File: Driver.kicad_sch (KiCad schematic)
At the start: 24 parts

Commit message: Тестовая версия
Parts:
- R7, R8: value 1.1k -> 10k
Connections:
- net E1 renamed OUT1
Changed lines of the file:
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@@
     )
   )
-  (global_label "E1" (shape input) (at 119.126 150.876 0) (fields_autoplaced)
-    (effects (font (size 1.27 1.27)) (justify left))
-    (property "Intersheet References" "${INTERSHEET_REFS}" (id 0) (at 123.8977 150.7966 0)
+  (global_label "OUT1" (shape input) (at 119.126 150.876 0) (fields_autoplaced)
+    (effects (font (size 1.27 1.27)) (justify left))
+    (property "Intersheet References" "${INTERSHEET_REFS}" (id 0) (at 126.3772 150.7966 0)
       (effects (font (size 1.27 1.27)) (justify left) hide)
     )
@@
     (in_bom yes) (on_board yes)
     (property "Reference" "R8" (id 0) (at 110.236 72.136 0))
-    (property "Value" "1.1k" (id 1) (at 105.918 72.136 90))
+    (property "Value" "10k" (id 1) (at 105.918 72.136 90))
     (property "Footprint" "Resistor_SMD:R_0805_2012Metric_Pad1.20x1.40mm_HandSolder" (id 2) (at 107.95 72.136 0)
       (effects (font (size 1.27 1.27)) hide)
@@
     (in_bom yes) (on_board yes)
     (property "Reference" "R7" (id 0) (at 105.664 148.59 90))
-    (property "Value" "1.1k" (id 1) (at 105.664 150.876 90))
+    (property "Value" "10k" (id 1) (at 105.664 150.876 90))
     (property "Footprint" "Resistor_SMD:R_0805_2012Metric_Pad1.20x1.40mm_HandSolder" (id 2) (at 105.664 150.876 0)
       (effects (font (size 1.27 1.27)) hide)

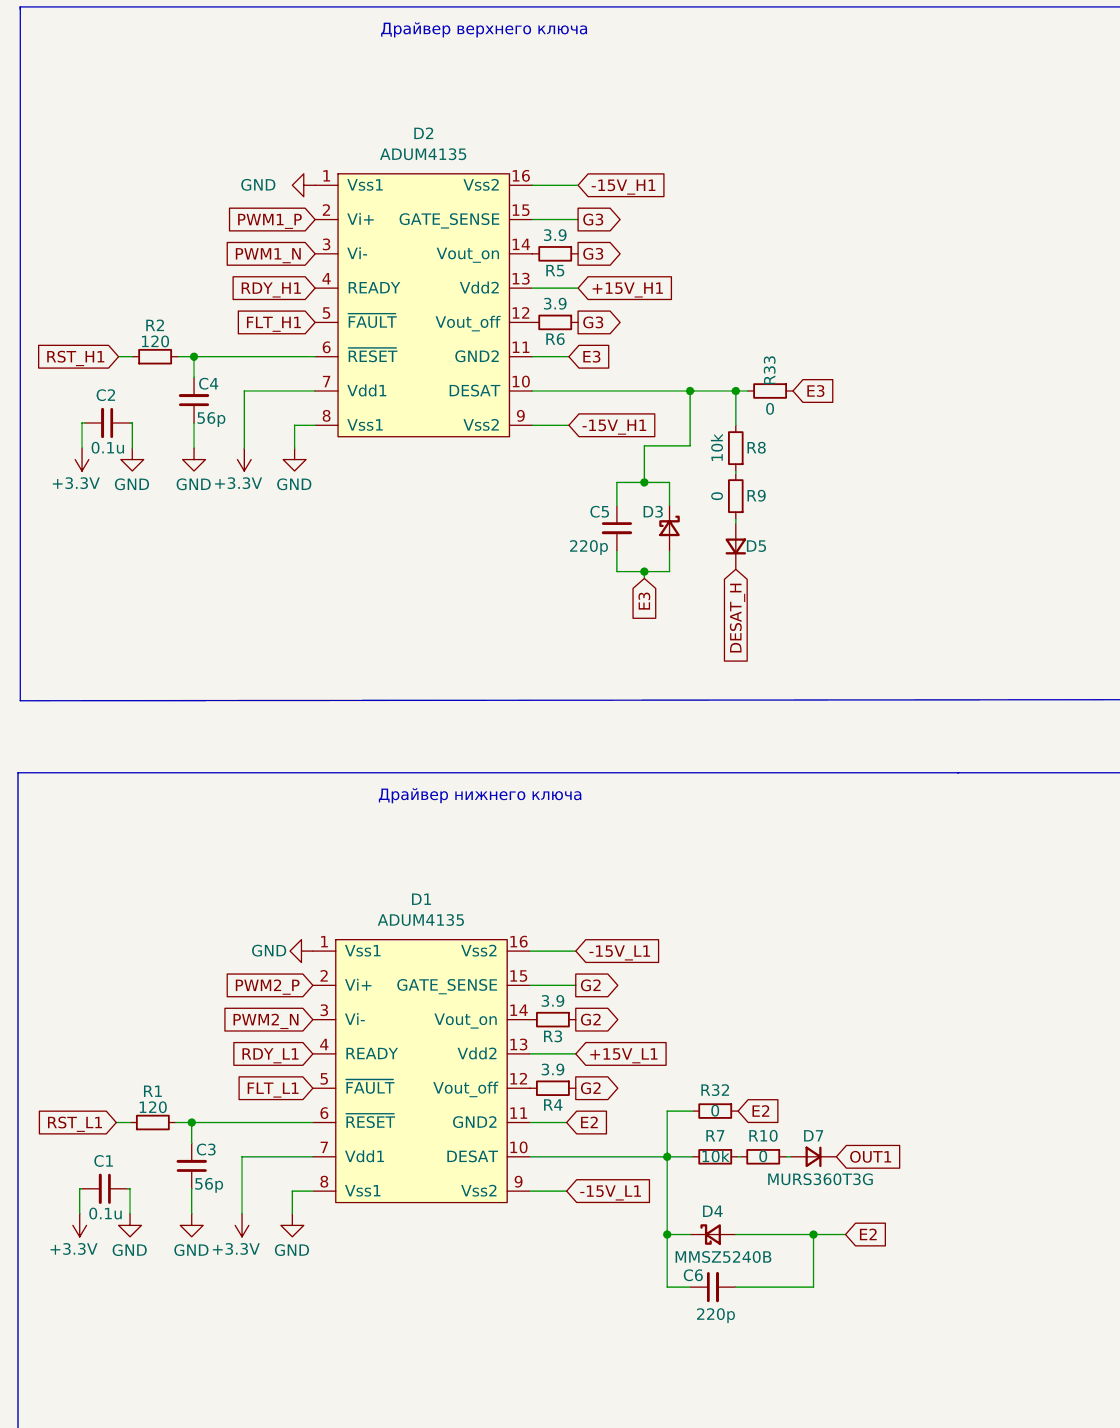
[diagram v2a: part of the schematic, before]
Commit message: Убрал питание 3.3В
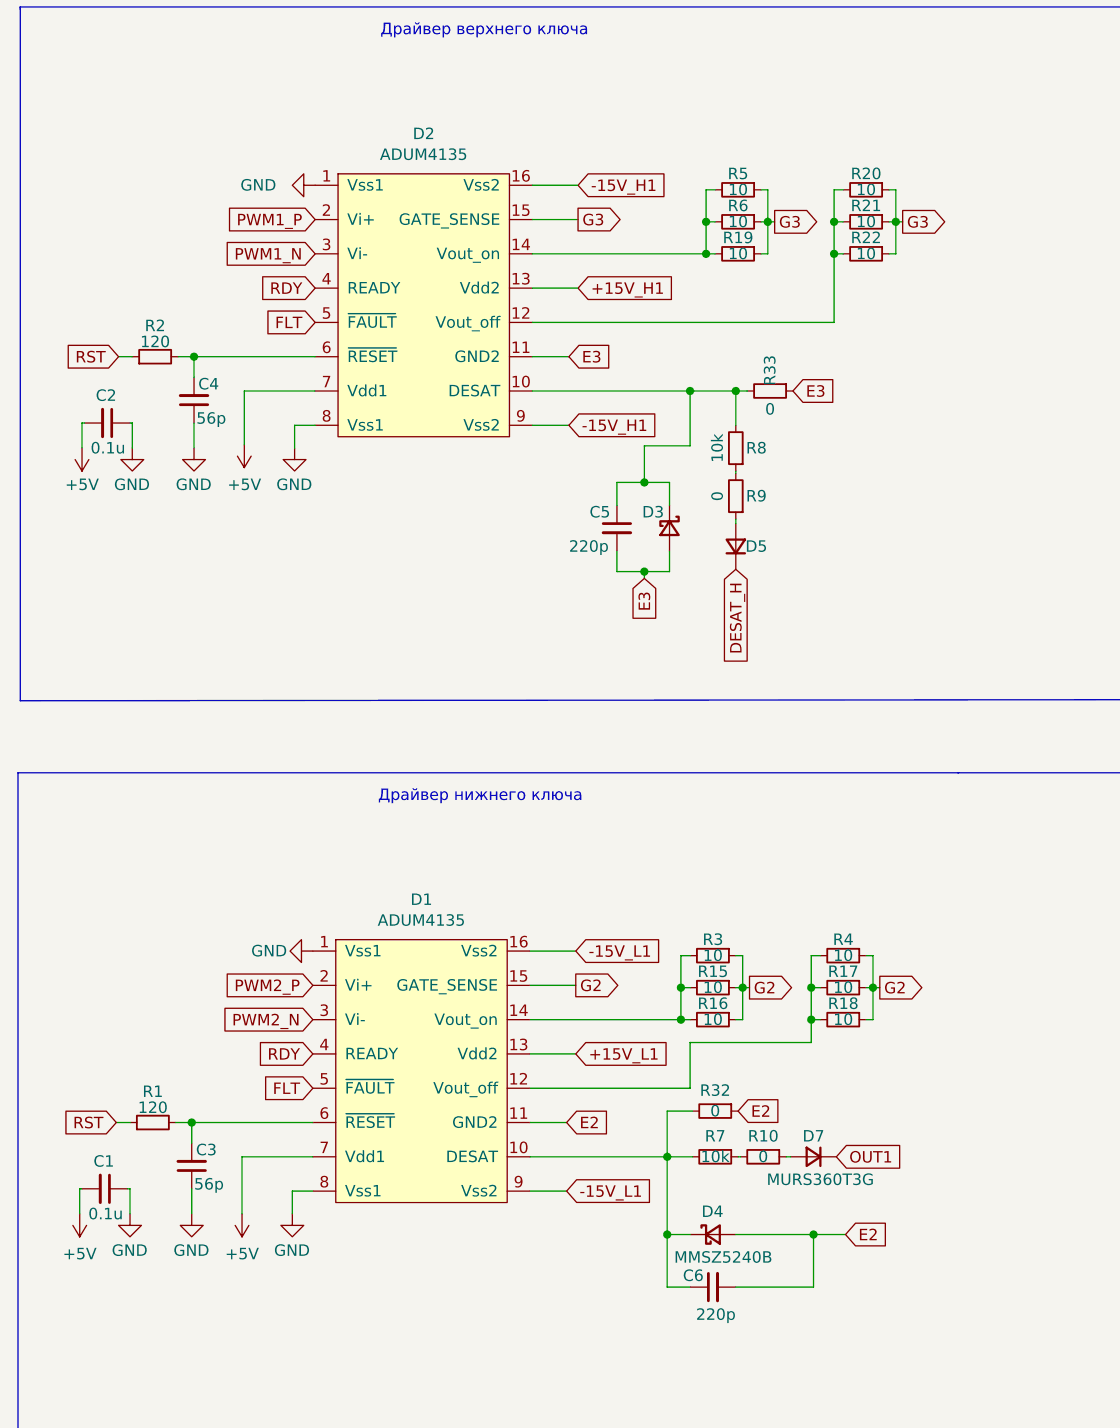
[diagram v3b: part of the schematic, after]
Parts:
- added R15, R16, R17, R18, R19, R20, R21, R22: 10, Resistor_SMD:R_1206_3216Metric_Pad1.30x1.75mm_HandSolder, symbol Device:R_Small
- D5, D7: footprint Diode_SMD:D_SMC -> Diode_SMD:D_SMA
- R3, R4, R5, R6: value 3.9 -> 10; footprint Resistor_SMD:R_2512_6332Metric_Pad1.40x3.35mm_HandSolder -> Resistor_SMD:R_1206_3216Metric_Pad1.30x1.75mm_HandSolder
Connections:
- net FLT_L1 is gone; now on net FLT: D1.5 (~{FAULT})
- net RDY_L1 is gone; now on net RDY: D1.4 (READY)
- net RST_L1 is gone; now on net RST: R1.1
- net G2: now also R15.1, R16.1, R17.1, R18.1
- net G3: now also R19.1, R20.1, R21.1, R22.1
- net at D2.12 (Vout_off): now also R20.2, R21.2, R22.2; no longer R6.2
- net at D1.14 (Vout_on), R3.2: now also R15.2, R16.2
- net at D2.14 (Vout_on), R5.2: now also R6.2, R19.2
- net at D1.12 (Vout_off), R4.2: now also R17.2, R18.2
- net +3V3 renamed +5V
- net FLT_H1 renamed FLT
- net RDY_H1 renamed RDY
- net RST_H1 renamed RST

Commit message: Развел все дорожки
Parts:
- removed R32, R33: 0, Resistor_SMD:R_0805_2012Metric_Pad1.20x1.40mm_HandSolder, symbol Device:R_Small
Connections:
- net +15V_H1 renamed +15V_H
- net +15V_L1 renamed +15V_L
- net -15V_H1 renamed -15V_H
- net -15V_L1 renamed -15V_L
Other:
- moved on the sheet: C5, C6, D4, D5, R15, R17, R20, R21, R3, R4, R5, R6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

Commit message: VER2.0 Отправил в резонит
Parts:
- removed D1, D2: ADUM4135, Package_SO:SOIC-16W_7.5x10.3mm_P1.27mm, symbol ADUM_Driver:ADUM4135
- added D1, D2: NSI6651ASC-DSWR, Package_SO:SOIC-16W_7.5x10.3mm_P1.27mm, symbol Driver_My:NSI6651
- D5, D7: value MURS360T3G -> MURS160
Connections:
- net +15V_H: now also D2.5 (Vcc2)
- net +15V_L: now also D1.5 (Vcc2)
- net +5V: now also D1.15 (Vcc1), D2.15 (Vcc1)
- net -15V_H: now also D2.1 (Vee2), D2.8 (Vee2)
- net -15V_L: now also D1.1 (Vee2), D1.8 (Vee2)
- net E2: now also D1.3 (GND2)
- net E3: now also D2.3 (GND2)
- net FLT: now also D1.13 (~{FLT}), D2.13 (~{FLT})
- net G2: now also D1.7 (CLAMP)
- net G3: now also D2.7 (CLAMP)
- net GND: now also D1.16 (TEST), D1.9 (GND1), D2.16 (TEST), D2.9 (GND1)
- net PWM1_N: now also D2.11 (IN-)
- net PWM1_P: now also D2.10 (IN+)
- net PWM2_N: now also D1.11 (IN-)
- net PWM2_P: now also D1.10 (IN+)
- net RDY: now also D1.12 (RDY), D2.12 (RDY)
- net at R20.2, R21.2, R22.2: now also D2.4 (OUTH)
- net at C5.1, D3.1 (K), R8.2: now also D2.2 (DESAT)
- net at R15.2, R16.2, R3.2: now also D1.6 (OUTL)
- net at R19.2, R5.2, R6.2: now also D2.6 (OUTL)
- net at C3.2, R1.2: now also D1.14 (~{RST})
- net at C6.1, D4.1 (K), R7.2: now also D1.2 (DESAT)
- net at C4.2, R2.2: now also D2.14 (~{RST})
- net at R17.2, R18.2, R4.2: now also D1.4 (OUTH)
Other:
- moved on the sheet: C3, C4, D5, D7, R10, R7, R8, R9

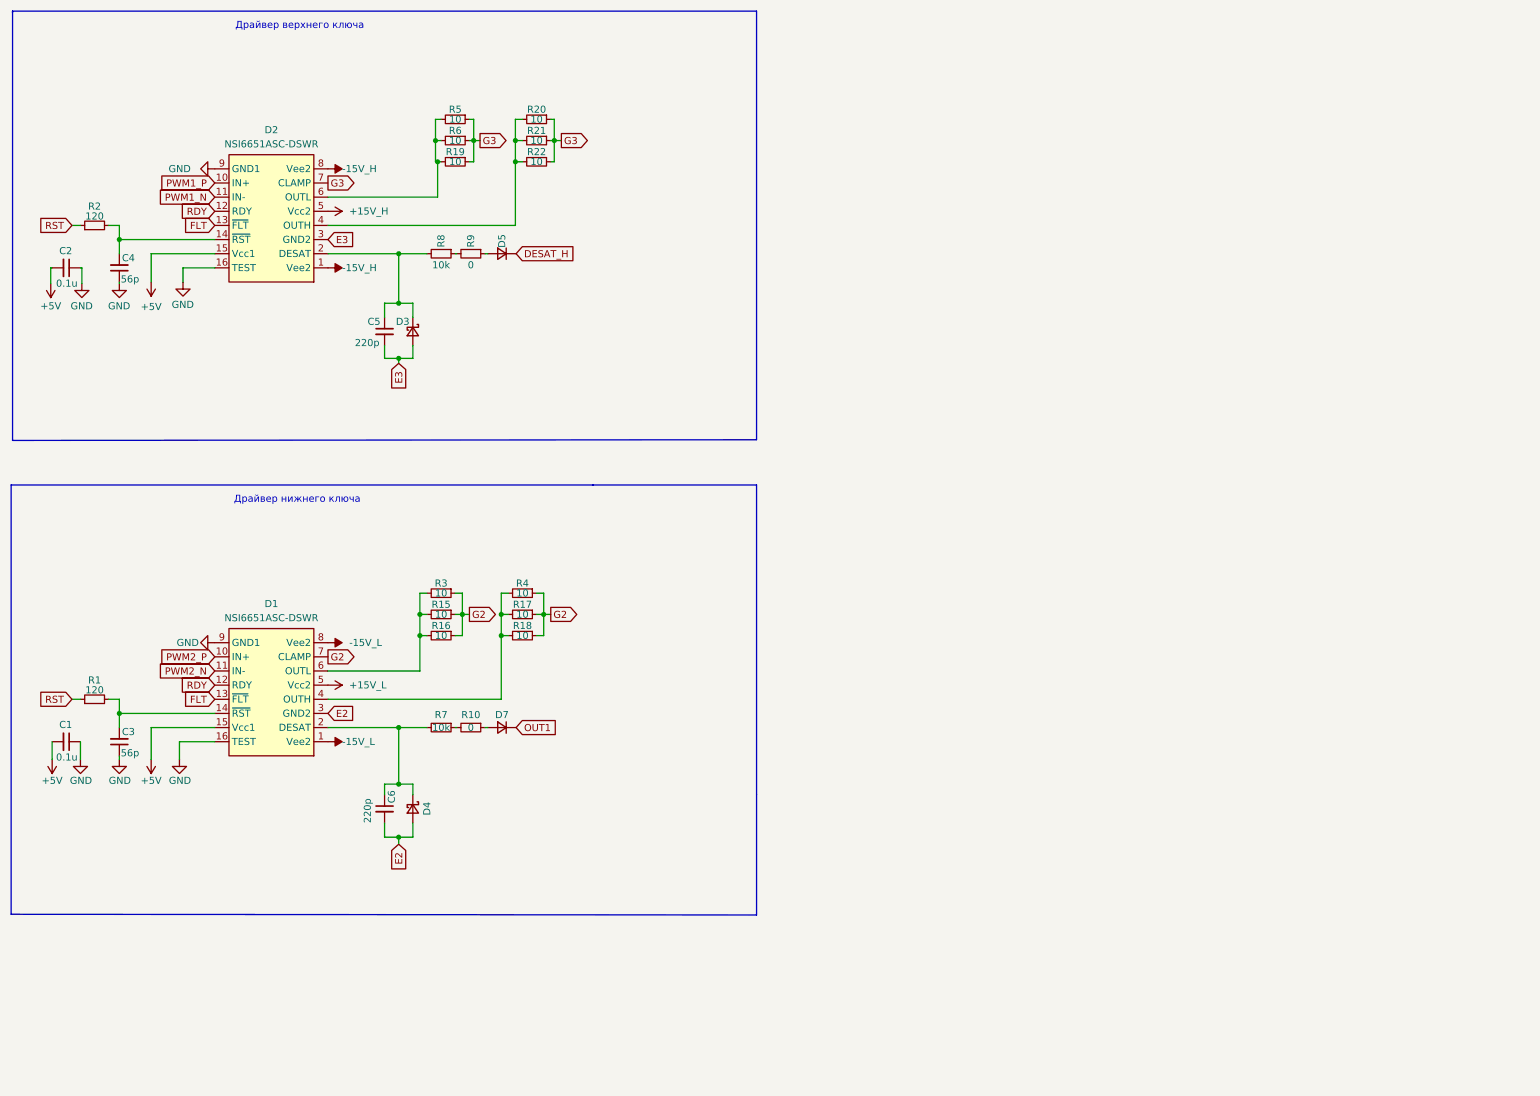
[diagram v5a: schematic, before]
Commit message: Изменения: добавил 5 вольтовые RS485 на вход драйверов
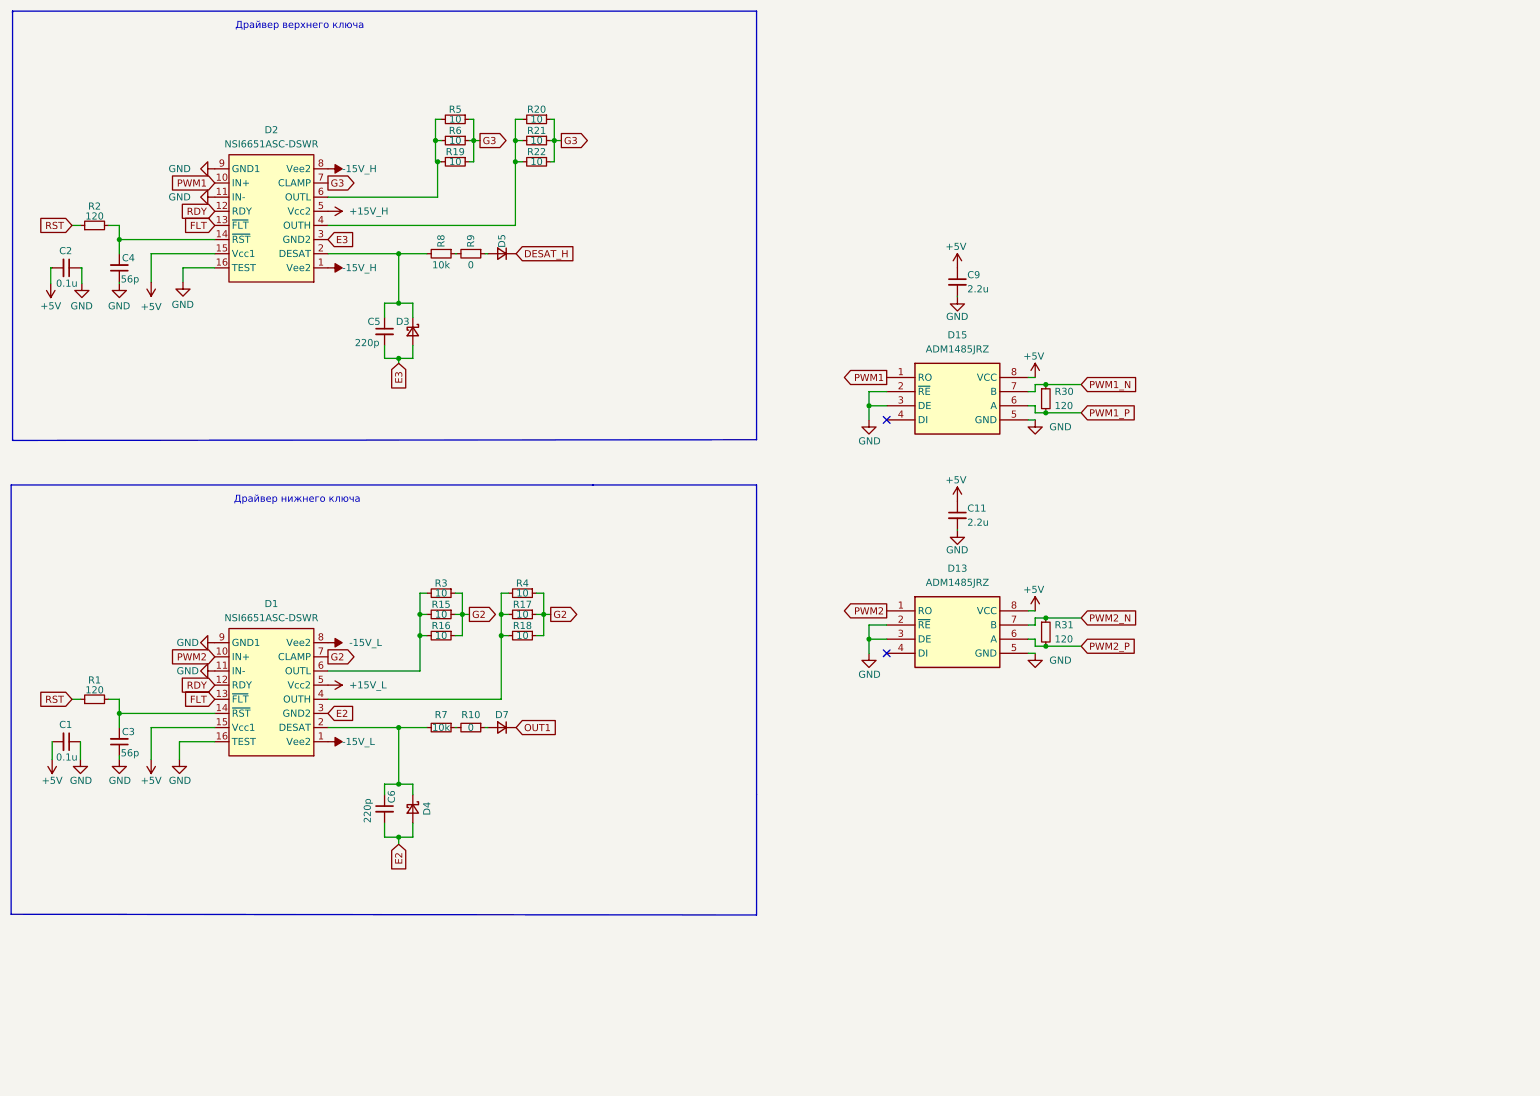
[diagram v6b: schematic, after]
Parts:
- added C11, C9: 2.2u, Capacitor_SMD:C_0805_2012Metric_Pad1.18x1.45mm_HandSolder, symbol Device:C_Small
- added D13, D15: ADM1485JRZ, Package_SO:SOIC-8_3.9x4.9mm_P1.27mm, symbol ADM1485JRZ:ADM1485JRZ
- added R30, R31: 120, Resistor_SMD:R_0805_2012Metric_Pad1.20x1.40mm_HandSolder, symbol Device:R_Small
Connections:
- net +5V: now also C11.1, C9.1, D13.8 (VCC), D15.8 (VCC)
- net GND: now also D1.11 (IN-), D2.11 (IN-), C11.2, C9.2, D13.2 (~{RE}), D13.3 (DE), D13.5 (GND), D15.2 (~{RE}), D15.3 (DE), D15.5 (GND)
- net PWM1_N: now also D15.7 (B), R30.1; no longer D2.11 (IN-)
- net PWM1_P: now also D15.6 (A), R30.2; no longer D2.10 (IN+)
- net PWM2_N: now also D13.7 (B), R31.1; no longer D1.11 (IN-)
- net PWM2_P: now also D13.6 (A), R31.2; no longer D1.10 (IN+)
- new net PWM1: D15.1 (RO), D2.10 (IN+)
- new net PWM2: D1.10 (IN+), D13.1 (RO)
- no-connect marks 0 -> 2
